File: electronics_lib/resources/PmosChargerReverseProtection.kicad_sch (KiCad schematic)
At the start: 4 parts

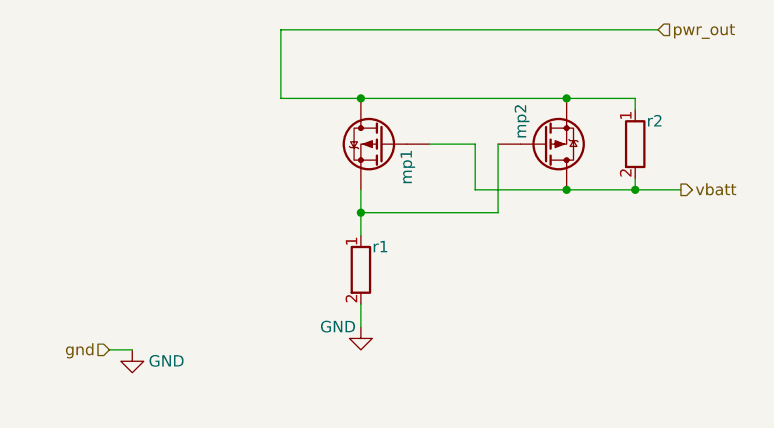
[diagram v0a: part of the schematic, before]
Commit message: Add: test_protected_charger for testing reverse protection Fix: revert test_pcbbot changes Fix: PMOS charger protection m1 being flipped
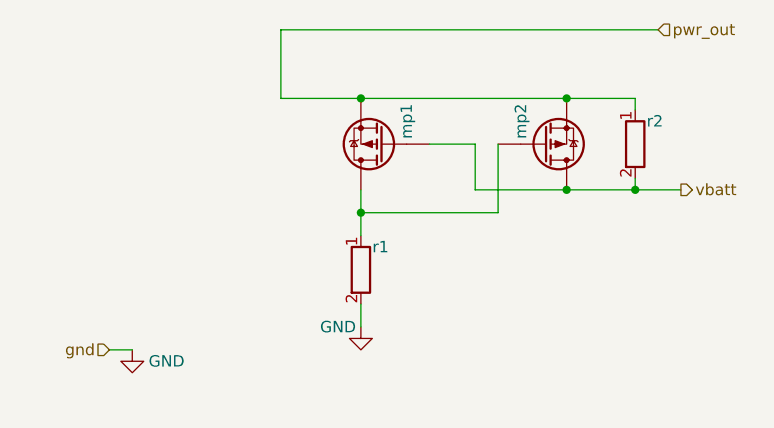
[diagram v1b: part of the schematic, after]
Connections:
- net pwr_out: now also mp1.3 (S); no longer mp1.1 (D)
- net at mp2.2 (G), r1.1: now also mp1.1 (D); no longer mp1.3 (S)
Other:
- moved on the sheet: mp1
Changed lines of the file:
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@@
-    (stroke (width 0) (type default))
-  )
-  (wire (pts (xy 152.4 83.82) (xy 152.4 86.36))
     (stroke (width 0) (type default))
   )
@@
     (stroke (width 0) (type default))
   )
-  (wire (pts (xy 143.51 73.66) (xy 152.4 73.66))
-    (stroke (width 0) (type default))
-  )
   (wire (pts (xy 124.46 101.6) (xy 127 101.6))
     (stroke (width 0) (type default))
@@
     (stroke (width 0) (type default))
   )
+  (wire (pts (xy 152.4 83.82) (xy 152.4 86.36))
+    (stroke (width 0) (type default))
+  )
   (wire (pts (xy 143.51 66.04) (xy 143.51 73.66))
+    (stroke (width 0) (type default))
+  )
+  (wire (pts (xy 143.51 73.66) (xy 152.4 73.66))
     (stroke (width 0) (type default))
   )
@@
     )
   )
-  (symbol (lib_id "Device:Q_PMOS_DGS") (at 154.94 78.74 0) (mirror y) (unit 1)
+  (symbol (lib_id "Device:Q_PMOS_DGS") (at 154.94 78.74 180) (unit 1)
     (in_bom yes) (on_board yes) (dnp no)
-    (property "Reference" "mp1" (at 157.48 81.28 90)
+    (property "Reference" "mp1" (at 157.48 76.2 90)
       (effects (font (size 1.27 1.27)))
     )
@@
       (effects (font (size 1.27 1.27)))
     )
-    (property "Footprint" "" (at 149.86 76.2 0)
+    (property "Footprint" "" (at 149.86 81.28 0)
       (effects (font (size 1.27 1.27)) hide)
     )

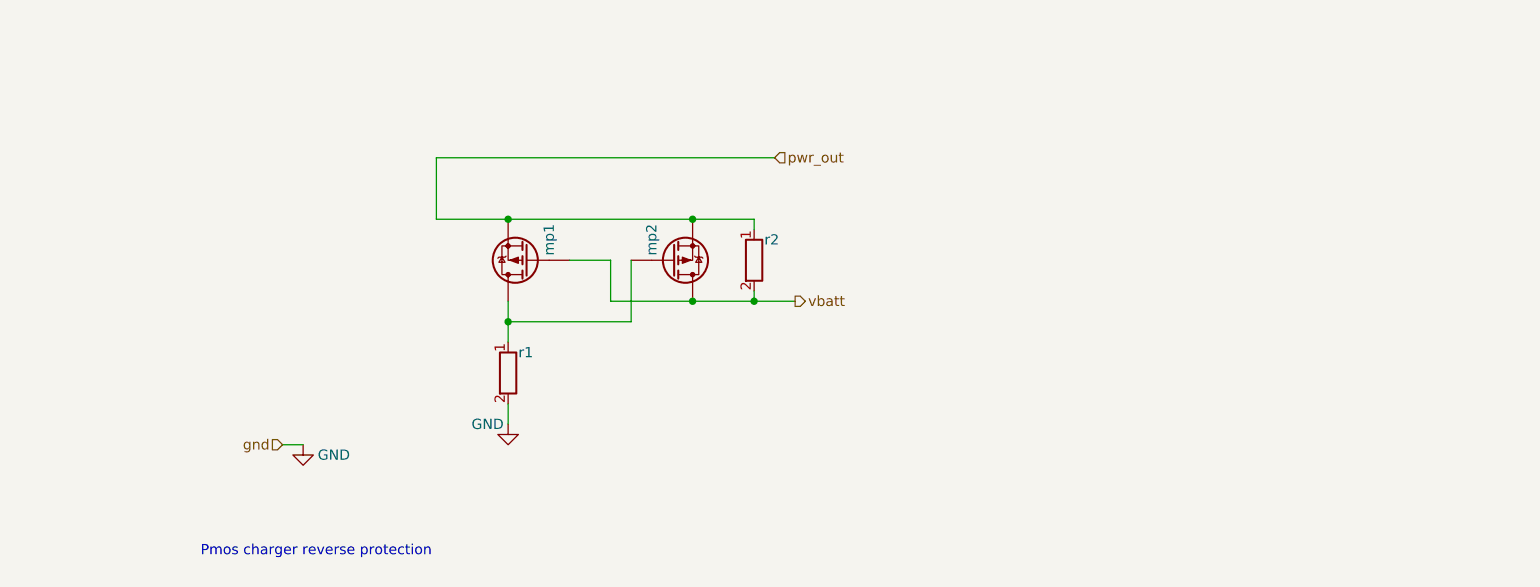
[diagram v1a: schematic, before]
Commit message: Update: comments in the schematics for Pmos Charger protection
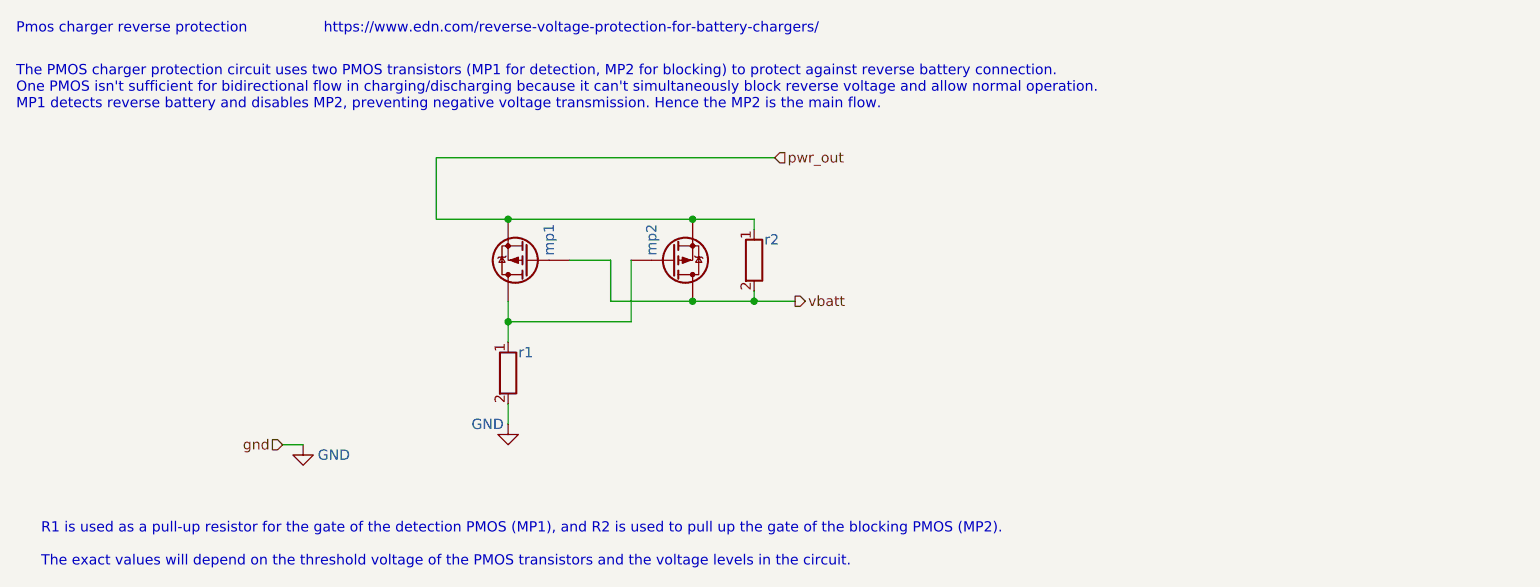
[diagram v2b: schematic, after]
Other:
- note added: "R1 is used as a pull-up resistor for the gate of the detection PMOS (MP1), and R2 is used to pull up the gate of the blocking PMOS (MP2). The exact values will depend on the threshold voltage of the PMOS transistors and the voltage levels in the circuit."
- note added: "The PMOS charger protection circuit uses two PMOS transistors (MP1 for detection, MP2 for blocking) to protect against reverse battery connection. One PMOS isn't sufficient for bidirectional flow in charging/discharging because it can't simultaneously block reverse voltage and allow normal operation. MP1 detects reverse battery and disables MP2, preventing negative voltage transmission. Hence the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"
- note added: "https://www.edn.com/reverse-voltage-protection-for-battery-chargers/"

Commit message: Add: pwr_in Fix: refactor the port names Add: docstring on the ports Update: mp1/mp2 to be based on the max on the voltage/current in both direction
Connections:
- net vbatt renamed pwr_in
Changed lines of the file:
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@@
     (effects (font (size 1.27 1.27)) (justify left))
   )
-  (hierarchical_label "vbatt" (shape output) (at 187.96 83.82 0) (fields_autoplaced)
+  (hierarchical_label "pwr_in" (shape output) (at 187.96 83.82 0) (fields_autoplaced)
     (effects (font (size 1.27 1.27)) (justify left))
   )
